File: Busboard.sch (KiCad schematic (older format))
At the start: 31 parts, among them J1 Conn_01x02, J10 Conn_02x08_Counter_Clockwise, J11 Conn_02x08_Counter_Clockwise, J12 Conn_01x02, J13 Conn_01x02, J14 Conn_01x02, J15 Conn_01x02, J16 Conn_02x08_Counter_Clockwise, J17 Conn_02x08_Counter_Clockwise, J18 Conn_02x08_Counter_Clockwise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

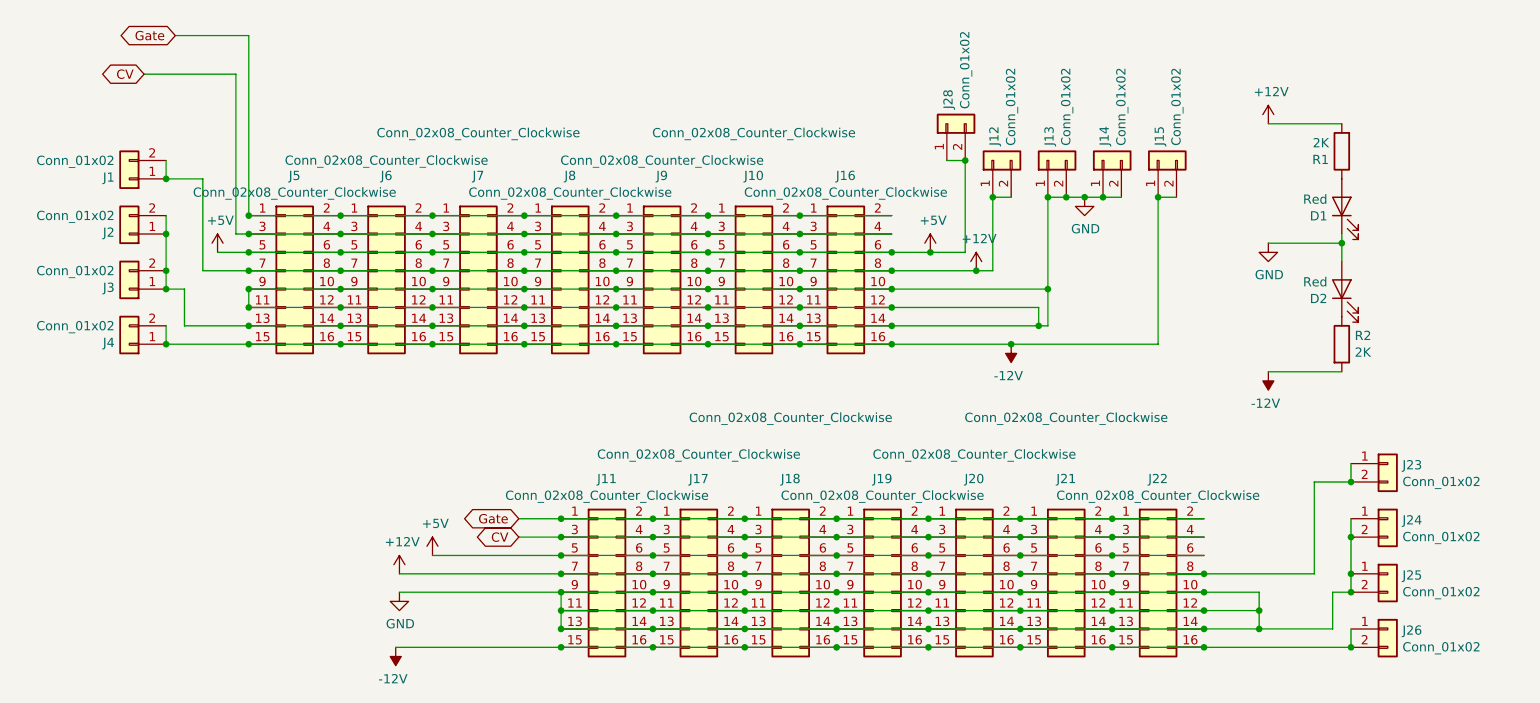
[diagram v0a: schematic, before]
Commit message: v02
Added jumpers for Gate and CV.
Changed to screw terminals.
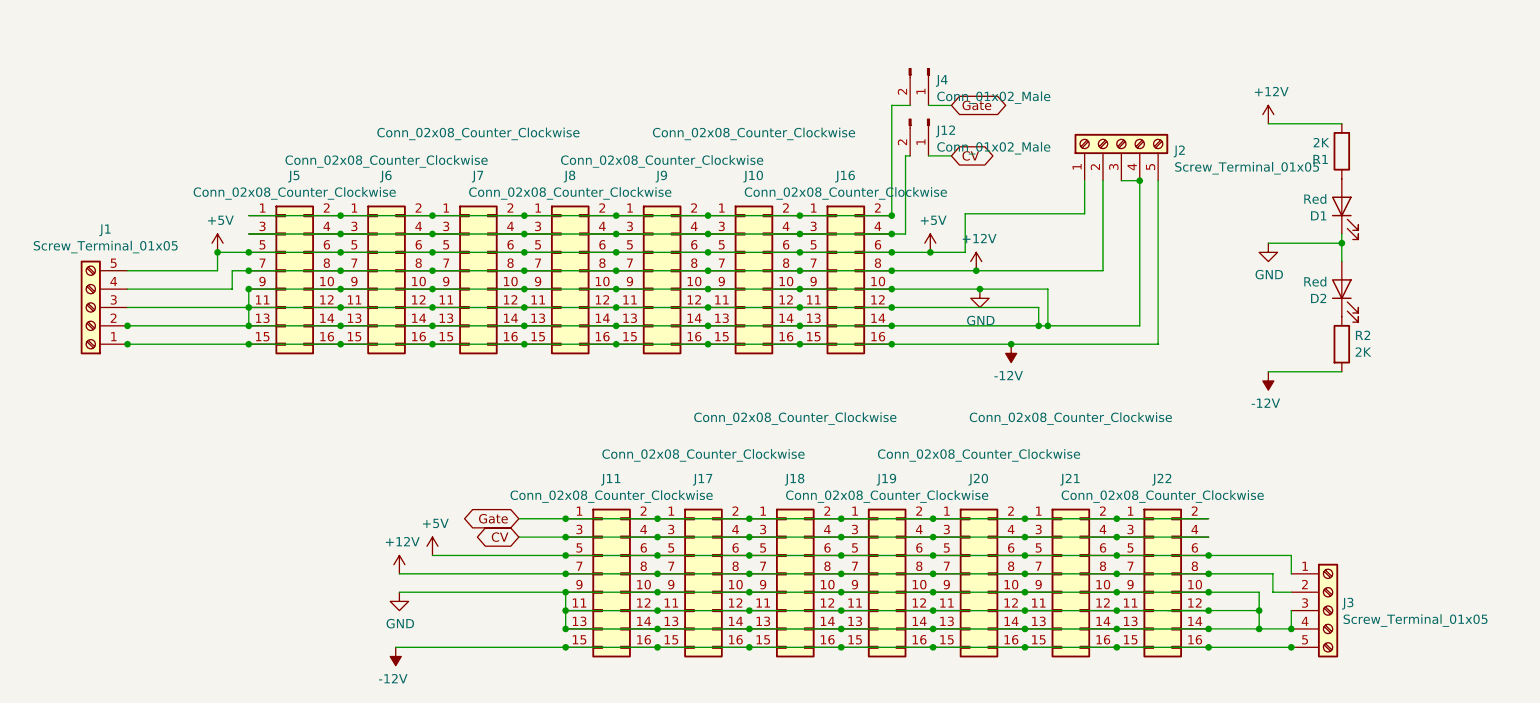
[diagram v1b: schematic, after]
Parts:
- removed J1, J12, J13, J14, J15, J2, J23, J24, J25, J26, J28, J3, J4: Conn_01x02, own_libraries:keystone-FASTON, symbol Connector_Generic:Conn_01x02
- added J1, J2, J3: Screw_Terminal_01x05, TerminalBlock_RND:TerminalBlock_RND_205-00048_1x05_P5.00mm_Horizontal, symbol Connector:Screw_Terminal_01x05
- added J12, J4: Conn_01x02_Male, Connector_PinHeader_2.54mm:PinHeader_1x02_P2.54mm_Vertical, symbol Connector:Conn_01x02_Male
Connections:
- wire segments 188 -> 184
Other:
- moved on the sheet: J11, J17, J18, J19, J20, J21, J22
